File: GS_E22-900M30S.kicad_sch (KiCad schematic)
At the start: 11 parts, among them J1 Barrel_Jack, J3 Raspberry_Pi_2_3, U2 LT1085CT-5-PBF, U3 E22-900M30S

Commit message: Add files via upload
updated schematic and pcb
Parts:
- removed U2: LT1085CT-5-PBF, TO220-3_T_LIT, symbol 2024-09-27_01-13-31:LT1085CT-5-PBF
- removed U3: E22-900M30S, mainboard:XCVR_E22-900M30S, symbol Mainboard:E22-900M30S
- added U1: LT1085-5.0, LT1085-5:TO220-3_T_LIT, symbol Regulator_Linear:LT1085-5.0
- added U2: E22-900M30S, E22-900M30S:XCVR_E22-900M30S, symbol E22-900M30S:E22-900M30S
- C1: value 22uF -> 10uF; footprint TAJC_AVX -> tantulum capacitor:TAJC_AVX
- C2: value 10uF -> 22uF; footprint TAJC_AVX -> tantulum capacitor:TAJC_AVX
- C3: value 22uF (Tantalum) -> 100nF
- C4: value 22uF (Tantalum) -> 10uF
- renumbered R8 to R2
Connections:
- net GND: now also U1.1 (GND), U2.1 (GND), U2.11 (GND), U2.12 (GND), U2.2 (GND), U2.20 (GND), U2.22 (GND), U2.3 (GND), U2.4 (GND), U2.5 (GND)
- net RF_BUSY: now also U2.14 (BUSY)
- net RF_CS: now also U2.19 (NSS)
- net RF_DIO1: now also U2.13 (DIO1)
- net RF_DIO2: now also U2.8 (DIO2)
- net RF_MISO: now also U2.16 (MISO)
- net RF_MOSI: now also U2.17 (MOSI)
- net RF_RESET: now also U2.15 (~{RST})
- net RF_RXEN: now also U2.6 (RXEN)
- net RF_SCK: now also U2.18 (SCK)
- net RF_TXEN: now also U2.7 (TXEN)
- net VCC: now also U1.3 (VI); no longer C2.1, C3.1, C4.1, D1.1 (K)
- new net V_RF: C2.1, C3.1, C4.1, D1.1 (K), U1.2 (VO), U2.10 (VCC), U2.9 (VCC)

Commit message: Add files via upload
updated both schematic and pcb.
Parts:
- removed R1: 10K, Resistor_SMD:R_0603_1608Metric, symbol Device:R_Small
- added R1: 10K, Resistor_SMD:R_0805_2012Metric_Pad1.20x1.40mm_HandSolder, symbol Device:R
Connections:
- net GND: now also R1.1
- net RF_RESET: now also R1.2
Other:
- note added: "Raspberry Pi"
- note added: "VCC(Vin max = 20V and Vin min = 6.5V)"
- note added: "V_RF = 5V"
- note added: "Voltage Regulator - 5V (Fixed)"
- note added: "Voltage rated = 25V Tolerace = +- 10% Operating temp = - 55C ~ 125C"
- note added: "io1,io2 - just for interrupt to save power pull rx tx high 3.3V"
- note removed: "io1,io2 just for interrupt to save power pull rx tx high 3.3V"
- moved on the sheet: C1, C2, C3, C4, D1, J1, J3, R2, U1, U2

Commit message: Add files via upload
Final schematic and PCB board
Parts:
- added J2, J4, J5: Conn_01x01, MountingHole:MountingHole_2.2mm_M2_DIN965_Pad, symbol Connector_Generic:Conn_01x01
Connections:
- net GND: now also J4.1 (Pin_1)
- net VCC: now also J5.1 (Pin_1)
- net V_RF: now also J2.1 (Pin_1)

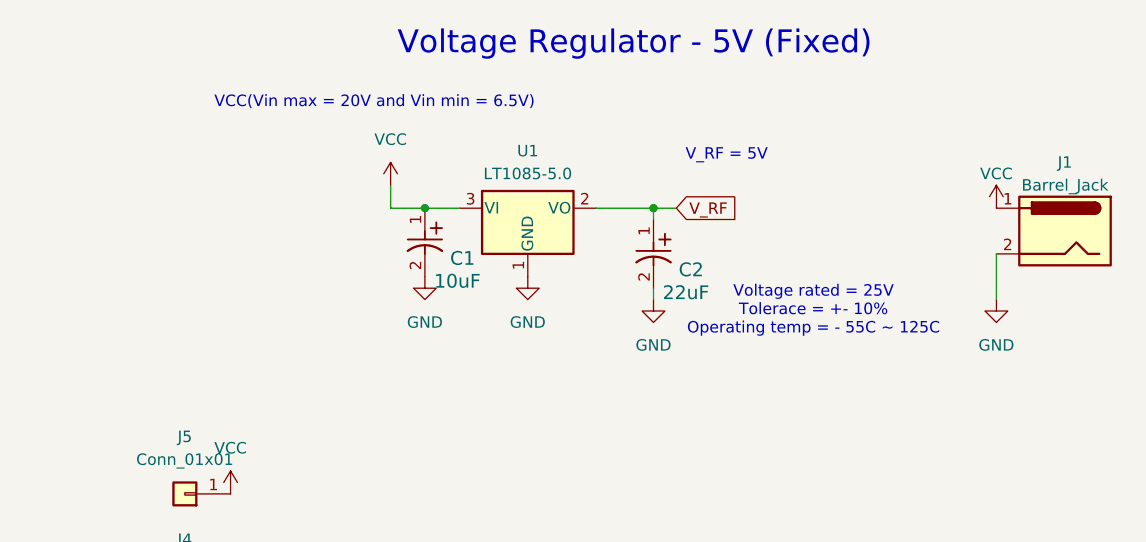
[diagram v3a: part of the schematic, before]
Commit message: Add files via upload
Hopefully this is the final version with the SMT voltage regulator with the new schematic as well.
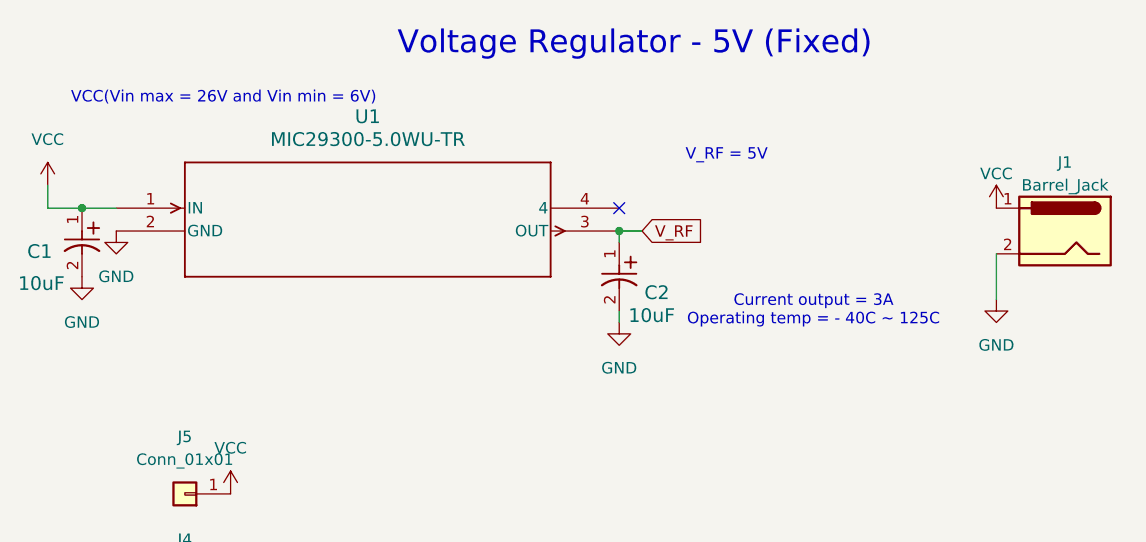
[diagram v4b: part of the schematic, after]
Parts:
- removed U1: LT1085-5.0, LT1085-5:TO220-3_T_LIT, symbol Regulator_Linear:LT1085-5.0
- added U1: MIC29300-5.0WU-TR, MIC29300_5:TO-263-3_MCH, symbol MIC29300_5_vol_reg:MIC29300-5.0WU-TR
- C2: value 22uF -> 10uF
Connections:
- net GND: now also U1.2 (GND)
- net VCC: now also U1.1 (IN)
- net V_RF: now also U1.3 (OUT)
- no-connect marks 23 -> 24
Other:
- note added: "Current output = 3A Operating temp = - 40C ~ 125C"
- note added: "VCC(Vin max = 26V and Vin min = 6V)"
- note removed: "VCC(Vin max = 20V and Vin min = 6.5V)"
- note removed: "Voltage rated = 25V Tolerace = +- 10% Operating temp = - 55C ~ 125C"
- moved on the sheet: C1, C2
